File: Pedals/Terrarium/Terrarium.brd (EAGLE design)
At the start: 59.4 x 57.8 mm, 43 parts, among them IC1 TL072CP, IC2 LM78L05

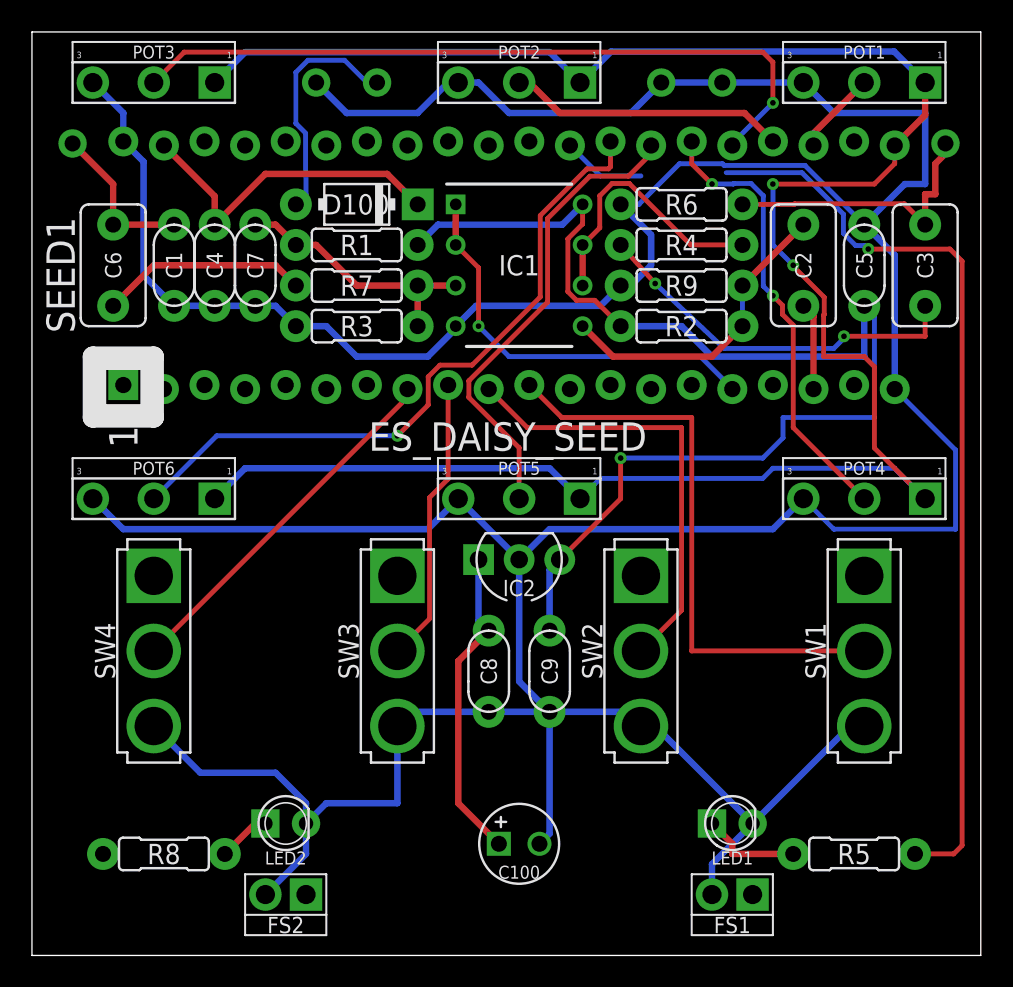
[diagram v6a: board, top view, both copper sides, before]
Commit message: Finished terrarium board routing
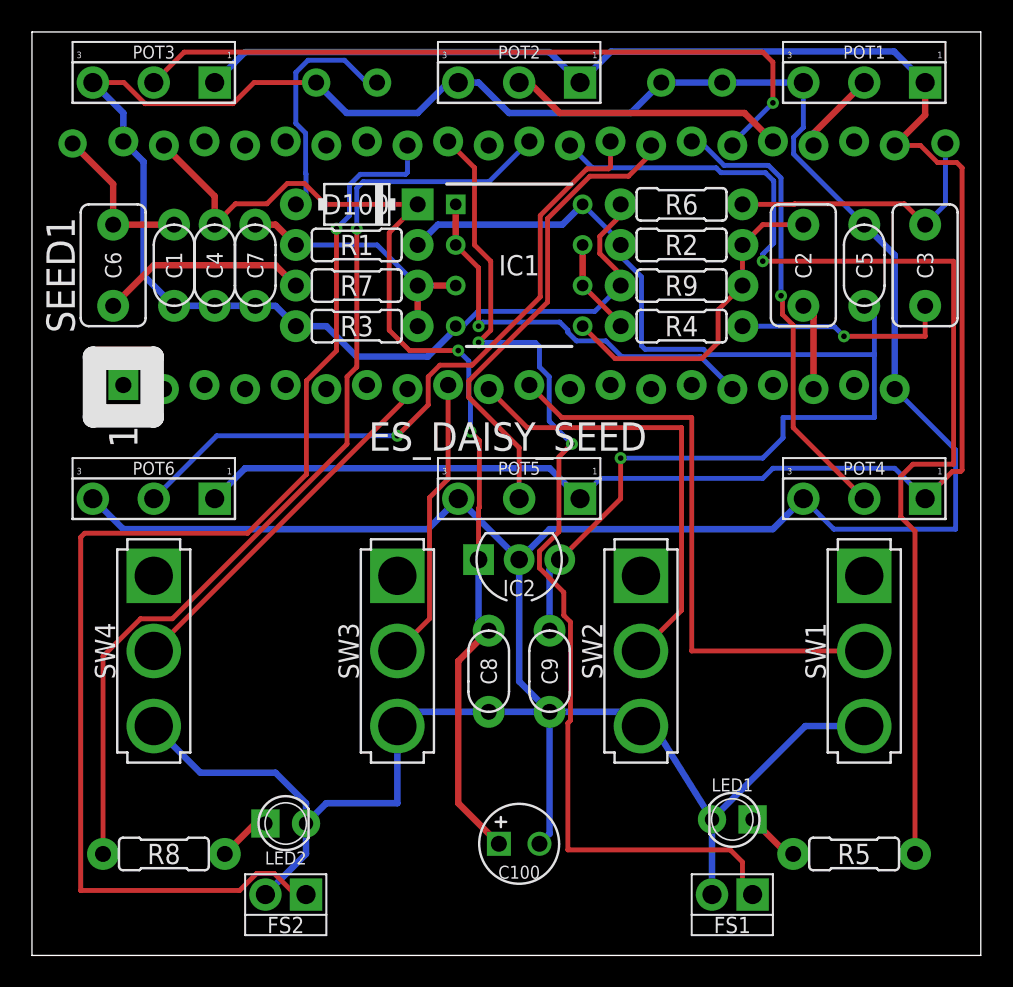
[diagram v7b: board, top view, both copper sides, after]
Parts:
- moved R2 5.08 mm to (40.6, 44.5)
- moved R4 5.08 mm to (40.6, 39.4), turned to 180 degrees
- moved LED1 0.25 mm to (43.8, 8.51), turned to 180 degrees
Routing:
- net FS2: track 0.00 -> 77.8 mm, vias 0 -> 1
- net FS1: track 0.00 -> 65.5 mm, vias 0 -> 2
- net LED2: track 0.00 -> 61.4 mm, vias 0 -> 1
- net VCC: track 41.0 -> 67.6 mm, vias 0 -> 2
- net N$14: track 16.9 -> 6.07 mm
- net GND: track 293.1 -> 282.5 mm
- net N$10: track 24.0 -> 13.6 mm, vias 2 -> 1
- net LED1: track 62.7 -> 71.2 mm
- net 3V3_A: track 134.4 -> 126.7 mm, vias 2 -> 0
- net +5V: track 78.2 -> 74.1 mm
- net N$7: track 6.24 -> 3.43 mm
- net N$17: track 19.5 -> 20.8 mm
- net N$4: track 28.3 -> 28.8 mm, vias 2 -> 1
